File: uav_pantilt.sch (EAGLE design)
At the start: 12 parts

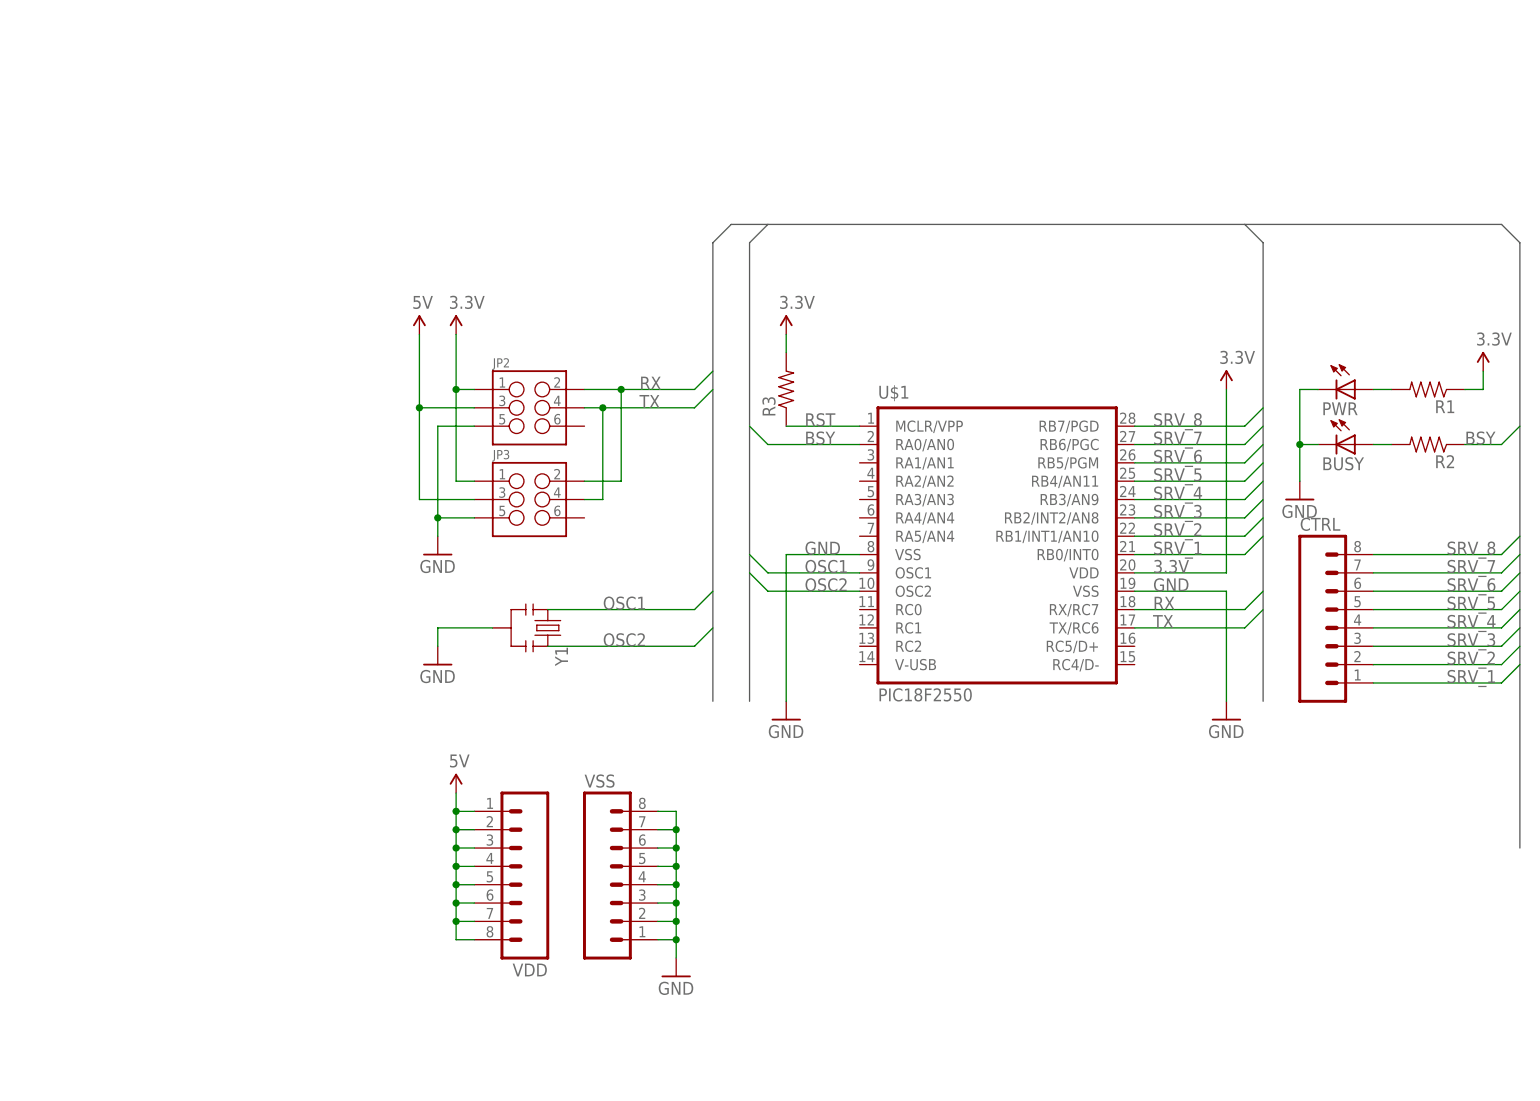
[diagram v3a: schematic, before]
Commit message: Adding ICSP to Pantilt board
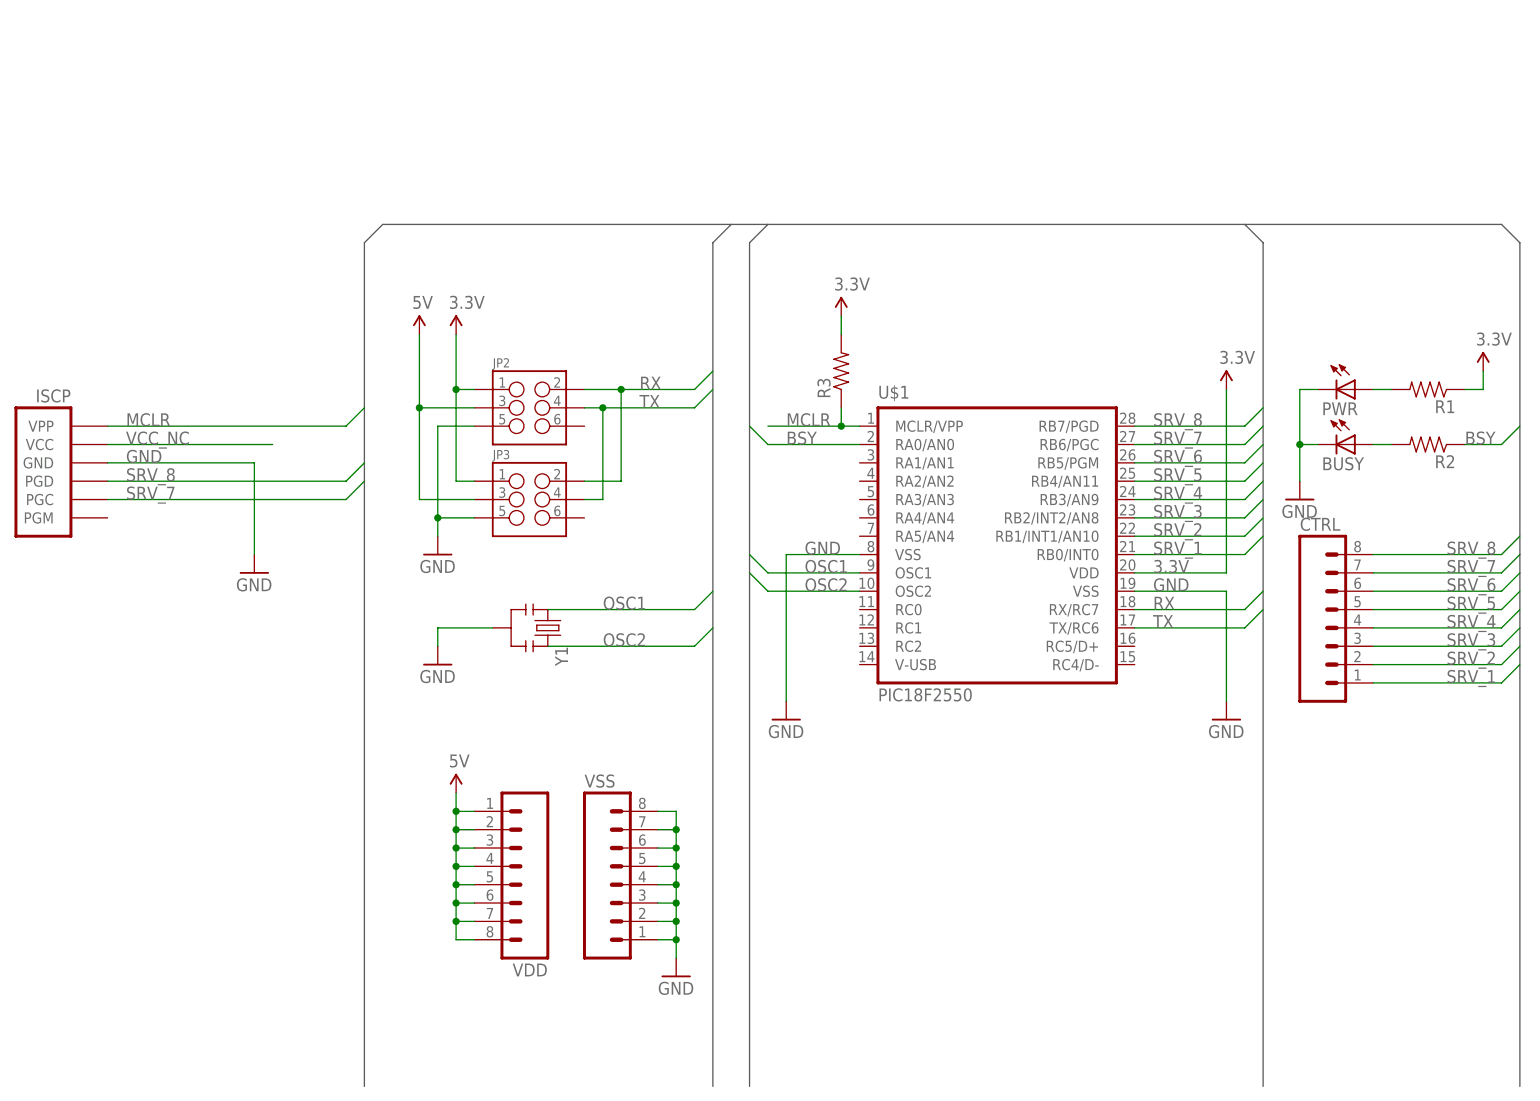
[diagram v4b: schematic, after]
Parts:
- added ISCP: PIC-ICSPPOLAR_LOCK, SparkFun-Connectors:PIC-ICSPPOLAR_LOCK
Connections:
- removed net RST: R3.1, U$1.MCLR/VPP
- new net MCLR: ISCP.VPP, R3.1, U$1.MCLR/VPP
- new net VCC_NC: ISCP.VCC
- net GND: now also ISCP.GND
- net SRV_7: now also ISCP.PGC
- net SRV_8: now also ISCP.PGD
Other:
- moved on the sheet: R3
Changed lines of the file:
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@@
 <part name="R3" library="SparkFun-Resistors" deviceset="RESISTOR" device="KIT"/>
 <part name="FRAME1" library="SparkFun-Aesthetics" deviceset="FRAME-A3" device=""/>
+<part name="ISCP" library="SparkFun-Connectors" deviceset="PIC-ICSP" device="POLAR_LOCK" value=""/>
+<part name="GND2" library="SparkFun-Aesthetics" deviceset="GND" device=""/>
 </parts>
 <sheets>
@@
 <instance part="U$1" gate="G$1" x="111.76" y="35.56"/>
 <instance part="SUPPLY1" gate="G$1" x="142.24" y="58.42"/>
-<instance part="SUPPLY2" gate="G$1" x="81.28" y="66.04"/>
+<instance part="SUPPLY2" gate="G$1" x="88.9" y="68.58"/>
 <instance part="GND1" gate="1" x="66.04" y="-22.86"/>
 <instance part="GND7" gate="1" x="152.4" y="43.18"/>
@@
 <instance part="BUSY" gate="G$1" x="160.02" y="50.8" rot="R270"/>
 <instance part="PWR" gate="G$1" x="160.02" y="58.42" rot="R270"/>
-<instance part="R3" gate="G$1" x="81.28" y="58.42" rot="R90"/>
+<instance part="R3" gate="G$1" x="88.9" y="60.96" rot="R90"/>
 <instance part="FRAME1" gate="G$1" x="-76.2" y="-93.98"/>
+<instance part="ISCP" gate="G$1" x="-20.32" y="48.26"/>
+<instance part="GND2" gate="1" x="7.62" y="33.02"/>
 </instances>
 <busses>
 <bus name="B$1">
 <segment>
-<wire x1="71.12" y1="78.74" x2="71.12" y2="15.24" width="0.762" layer="92"/>
+<wire x1="71.12" y1="78.74" x2="71.12" y2="-38.1" width="0.762" layer="92"/>
 <wire x1="71.12" y1="78.74" x2="73.66" y2="81.28" width="0.762" layer="92"/>
 <wire x1="73.66" y1="81.28" x2="78.74" y2="81.28" width="0.762" layer="92"/>
@@
 <wire x1="144.78" y1="81.28" x2="180.34" y2="81.28" width="0.762" layer="92"/>
 <wire x1="180.34" y1="81.28" x2="182.88" y2="78.74" width="0.762" layer="92"/>
-<wire x1="182.88" y1="78.74" x2="182.88" y2="-5.08" width="0.762" layer="92"/>
+<wire x1="182.88" y1="78.74" x2="182.88" y2="-38.1" width="0.762" layer="92"/>
 <wire x1="78.74" y1="81.28" x2="76.2" y2="78.74" width="0.762" layer="92"/>
-<wire x1="76.2" y1="78.74" x2="76.2" y2="15.24" width="0.762" layer="92"/>
-<wire x1="147.32" y1="15.24" x2="147.32" y2="78.74" width="0.762" layer="92"/>
+<wire x1="76.2" y1="78.74" x2="76.2" y2="-38.1" width="0.762" layer="92"/>
+<wire x1="147.32" y1="-38.1" x2="147.32" y2="78.74" width="0.762" layer="92"/>
 <wire x1="147.32" y1="78.74" x2="144.78" y2="81.28" width="0.762" layer="92"/>
+<wire x1="73.66" y1="81.28" x2="25.4" y2="81.28" width="0.762" layer="92"/>
+<wire x1="25.4" y1="81.28" x2="22.86" y2="78.74" width="0.762" layer="92"/>
+<wire x1="22.86" y1="78.74" x2="22.86" y2="-38.1" width="0.762" layer="92"/>
 </segment>
 </bus>
@@
 <pinref part="R3" gate="G$1" pin="2"/>
 <pinref part="SUPPLY2" gate="G$1" pin="3.3V"/>
-<wire x1="81.28" y1="66.04" x2="81.28" y2="63.5" width="0.1524" layer="91"/>
+<wire x1="88.9" y1="68.58" x2="88.9" y2="66.04" width="0.1524" layer="91"/>
 </segment>
 </net>
@@
 <junction x="152.4" y="50.8"/>
 </segment>
+<segment>
+<pinref part="ISCP" gate="G$1" pin="GND"/>
+<pinref part="GND2" gate="1" pin="GND"/>
+<wire x1="-12.7" y1="48.26" x2="7.62" y2="48.26" width="0.1524" layer="91"/>
+<wire x1="7.62" y1="48.26" x2="7.62" y2="35.56" width="0.1524" layer="91"/>
+<label x="-10.16" y="48.26" size="1.778" layer="95"/>
+</segment>
 </net>
 <net name="5V" class="0">
@@
 <label x="172.72" y="33.02" size="1.778" layer="95"/>
 </segment>
+<segment>
+<pinref part="ISCP" gate="G$1" pin="PGC"/>
+<wire x1="-12.7" y1="43.18" x2="20.32" y2="43.18" width="0.1524" layer="91"/>
+<label x="-10.16" y="43.18" size="1.778" layer="95"/>
+<wire x1="20.32" y1="43.18" x2="22.86" y2="45.72" width="0.1524" layer="91"/>
+</segment>
 </net>
 <net name="SRV_8" class="0">
@@
 <label x="172.72" y="35.56" size="1.778" layer="95"/>
 </segment>
+<segment>
+<pinref part="ISCP" gate="G$1" pin="PGD"/>
+<wire x1="-12.7" y1="45.72" x2="20.32" y2="45.72" width="0.1524" layer="91"/>
+<label x="-10.16" y="45.72" size="1.778" layer="95"/>
+<wire x1="20.32" y1="45.72" x2="22.86" y2="48.26" width="0.1524" layer="91"/>
+</segment>
 </net>
 <net name="N$1" class="0">
@@
 </segment>
 </net>
-<net name="RST" class="0">
-<segment>
-<pinref part="U$1" gate="G$1" pin="MCLR/VPP"/>
-<pinref part="R3" gate="G$1" pin="1"/>
-<wire x1="81.28" y1="53.34" x2="91.44" y2="53.34" width="0.1524" layer="91"/>
-<label x="83.82" y="53.34" size="1.778" layer="95"/>
-</segment>
-</net>
 <net name="BSY" class="0">
 <segment>
@@
 <wire x1="91.44" y1="50.8" x2="78.74" y2="50.8" width="0.1524" layer="91"/>
 <wire x1="78.74" y1="50.8" x2="76.2" y2="53.34" width="0.1524" layer="91"/>
-<label x="83.82" y="50.8" size="1.778" layer="95"/>
+<label x="81.28" y="50.8" size="1.778" layer="95"/>
 </segment>
 <segment>
@@
 </segment>
 </net>
+<net name="MCLR" class="0">
+<segment>
+<pinref part="ISCP" gate="G$1" pin="VPP"/>
+<wire x1="-12.7" y1="53.34" x2="20.32" y2="53.34" width="0.1524" layer="91"/>
+<label x="-10.16" y="53.34" size="1.778" layer="95"/>
+<wire x1="20.32" y1="53.34" x2="22.86" y2="55.88" width="0.1524" layer="91"/>
+</segment>
+<segment>
+<pinref part="U$1" gate="G$1" pin="MCLR/VPP"/>
+<pinref part="R3" gate="G$1" pin="1"/>
+<wire x1="88.9" y1="53.34" x2="91.44" y2="53.34" width="0.1524" layer="91"/>
+<label x="81.28" y="53.34" size="1.778" layer="95"/>
+<wire x1="88.9" y1="55.88" x2="88.9" y2="53.34" width="0.1524" layer="91"/>
+<wire x1="88.9" y1="53.34" x2="78.74" y2="53.34" width="0.1524" layer="91"/>
+<junction x="88.9" y="53.34"/>
+</segment>
+</net>
+<net name="VCC_NC" class="0">
+<segment>
+<pinref part="ISCP" gate="G$1" pin="VCC"/>
+<wire x1="-12.7" y1="50.8" x2="10.16" y2="50.8" width="0.1524" layer="91"/>
+<label x="-10.16" y="50.8" size="1.778" layer="95"/>
+</segment>
+</net>
